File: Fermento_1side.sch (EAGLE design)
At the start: 25 parts, among them Q1 32.768kHz, Q2 P-MOSFET

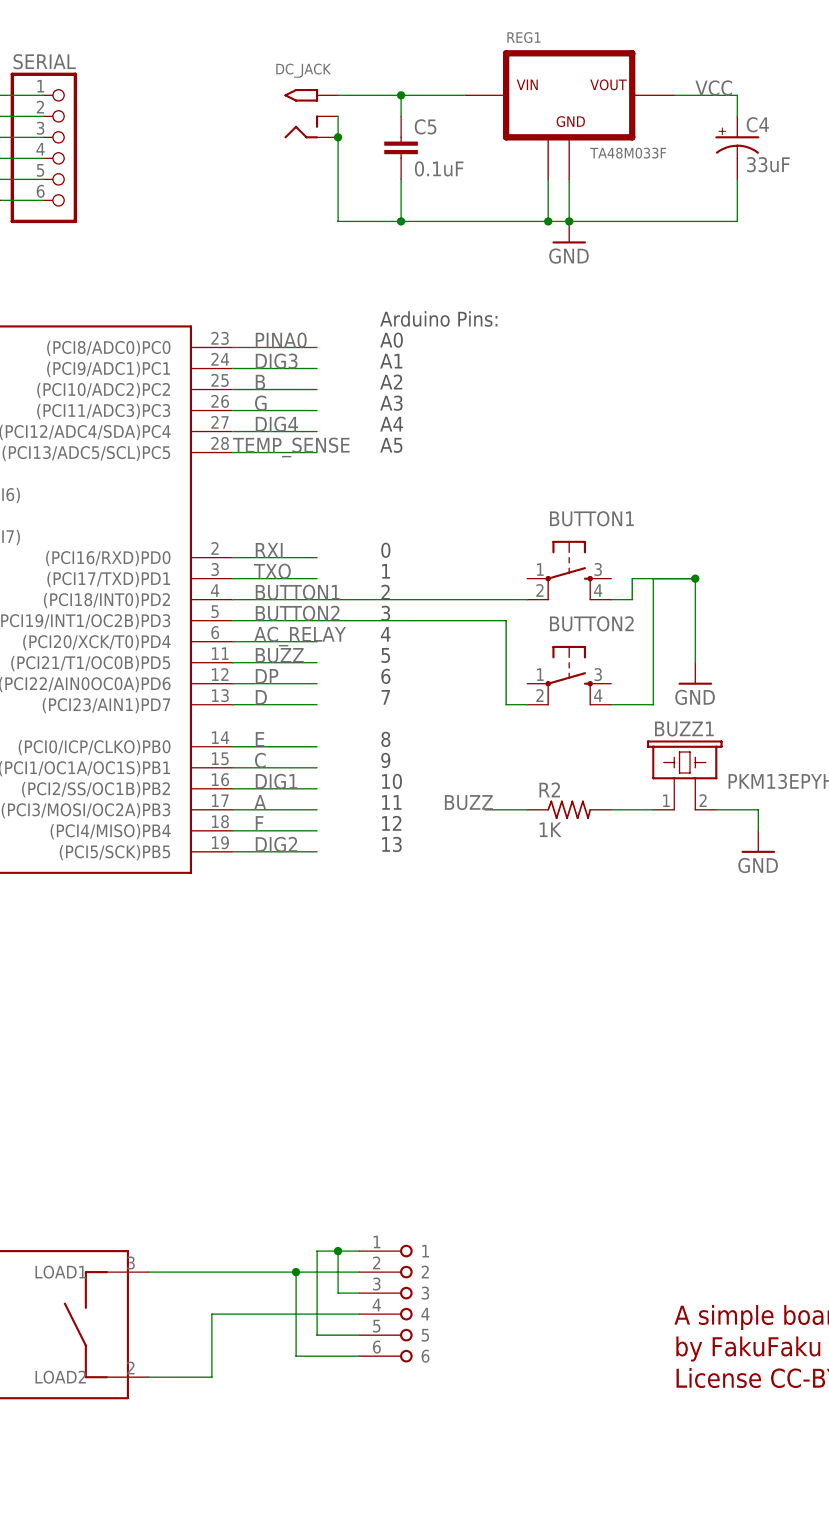
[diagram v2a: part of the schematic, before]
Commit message: One sided homebrew-friendly design redone.
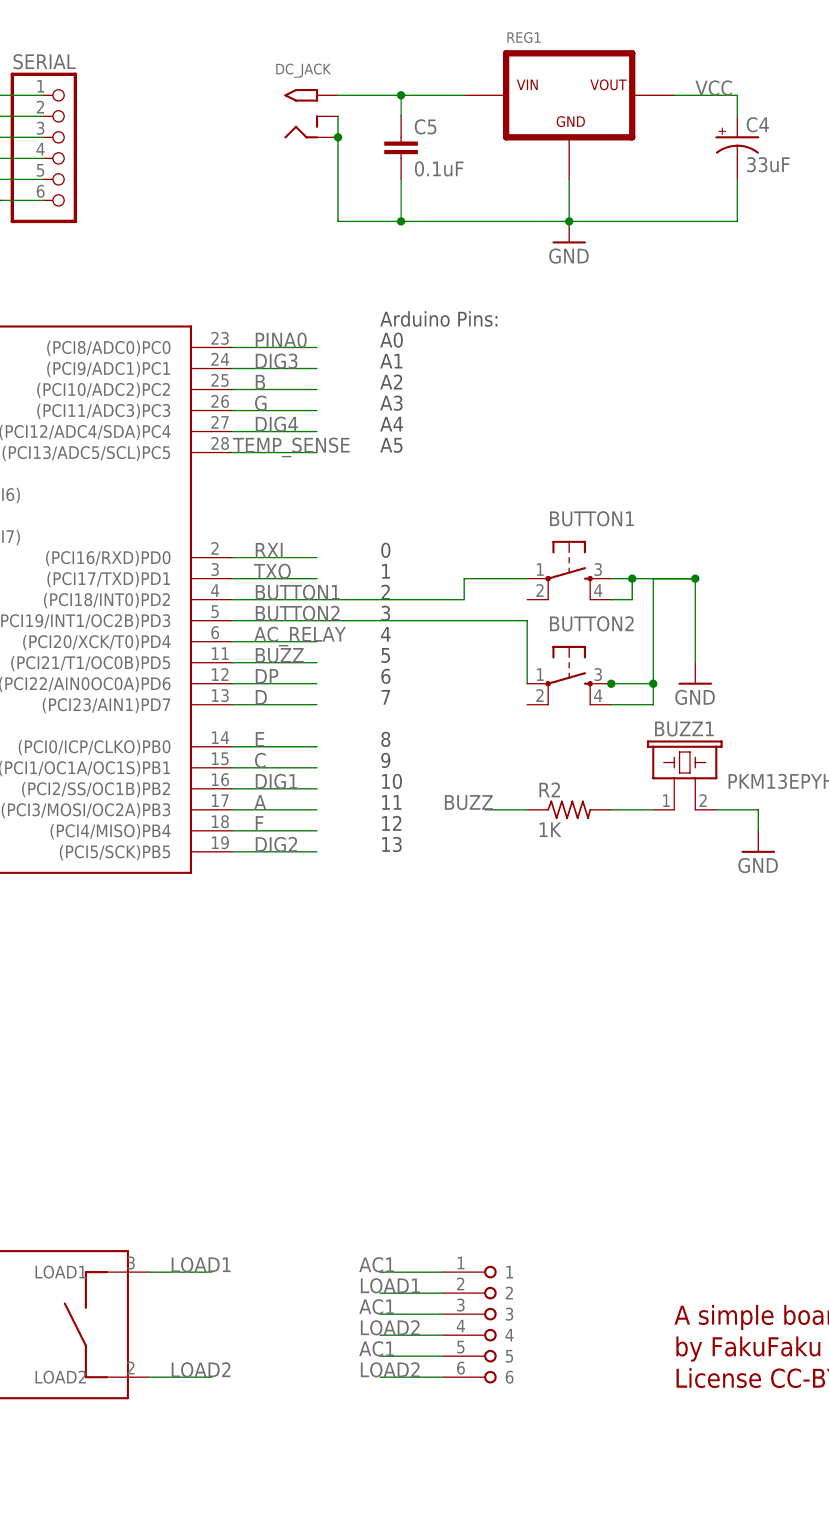
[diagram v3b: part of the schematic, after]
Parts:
- REG1: value TA48M033F -> REGULATOR-NOTHERMAL-TO220-STRAIGHT; device Robin:REGULATOR-TO-220 -> Robin:REGULATOR-NOTHERMAL-TO220-STRAIGHT
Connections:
- net N$5 renamed AC1
- removed net N$6: AC_RELAY.LOAD1, U$2.2, U$2.6
- removed net N$8: AC_RELAY.LOAD2, U$2.4
- new net LOAD1: AC_RELAY.LOAD1, U$2.2
- new net LOAD2: AC_RELAY.LOAD2, U$2.4, U$2.6
- net BUTTON1: now also BUTTON1.1; no longer BUTTON1.2
- net BUTTON2: now also BUTTON2.1; no longer BUTTON2.2
- net GND: now also BUTTON1.3, BUTTON2.3; no longer REG1.GND@1
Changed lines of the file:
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@@
 <part name="GND5" library="SparkFun" deviceset="GND" device=""/>
 <part name="GND6" library="SparkFun" deviceset="GND" device=""/>
-<part name="REG1" library="Robin" deviceset="REGULATOR" device="-TO-220" value="TA48M033F"/>
 <part name="C4" library="SparkFun" deviceset="CAP_POL" device="PTH2" value="33uF"/>
 <part name="C5" library="SparkFun" deviceset="CAP" device="PTH" value="0.1uF"/>
@@
 <part name="P+1" library="SparkFun" deviceset="VCC" device=""/>
 <part name="R3" library="adafruit" deviceset="R-US_" device="0207/10" value="10K"/>
+<part name="REG1" library="Robin" deviceset="REGULATOR-NOTHERMAL" device="-TO220-STRAIGHT" value=""/>
 </parts>
 <sheets>
@@
 <instance part="GND5" gate="1" x="231.14" y="-40.64"/>
 <instance part="GND6" gate="1" x="63.5" y="-27.94"/>
-<instance part="REG1" gate="G$1" x="154.94" y="-25.4"/>
 <instance part="C4" gate="G$1" x="175.26" y="-30.48"/>
 <instance part="C5" gate="G$1" x="134.62" y="-33.02"/>
@@
 <instance part="FRAME1" gate="G$2" x="165.1" y="-205.74"/>
 <instance part="AC_RELAY" gate="G$1" x="86.36" y="-175.26"/>
-<instance part="U$2" gate="G$1" x="134.62" y="-172.72"/>
+<instance part="U$2" gate="G$1" x="144.78" y="-175.26"/>
 <instance part="GND9" gate="1" x="66.04" y="-190.5"/>
 <instance part="H1" gate="G$1" x="55.88" y="-205.74"/>
@@
 <instance part="P+1" gate="1" x="55.88" y="-149.86"/>
 <instance part="R3" gate="G$1" x="40.64" y="-154.94" rot="R90"/>
+<instance part="REG1" gate="G$1" x="154.94" y="-25.4"/>
 </instances>
 <busses>
@@
 <pinref part="BUTTON2" gate="S" pin="4"/>
 <wire x1="160.02" y1="-99.06" x2="165.1" y2="-99.06" width="0.1524" layer="91"/>
-<wire x1="165.1" y1="-99.06" x2="165.1" y2="-83.82" width="0.1524" layer="91"/>
+<wire x1="165.1" y1="-99.06" x2="165.1" y2="-96.52" width="0.1524" layer="91"/>
+<wire x1="165.1" y1="-96.52" x2="165.1" y2="-83.82" width="0.1524" layer="91"/>
 <wire x1="165.1" y1="-83.82" x2="170.18" y2="-83.82" width="0.1524" layer="91"/>
 <pinref part="BUTTON1" gate="S" pin="4"/>
@@
 <wire x1="162.56" y1="-86.36" x2="162.56" y2="-83.82" width="0.1524" layer="91"/>
 <wire x1="162.56" y1="-83.82" x2="170.18" y2="-83.82" width="0.1524" layer="91"/>
+<junction x="162.56" y="-83.82"/>
+<junction x="165.1" y="-96.52"/>
+<pinref part="BUTTON2" gate="S" pin="3"/>
+<junction x="160.02" y="-96.52"/>
+<wire x1="160.02" y1="-96.52" x2="165.1" y2="-96.52" width="0.1524" layer="91"/>
+<pinref part="BUTTON1" gate="S" pin="3"/>
+<wire x1="162.56" y1="-83.82" x2="160.02" y2="-83.82" width="0.1524" layer="91"/>
 </segment>
 <segment>
@@
 <wire x1="175.26" y1="-40.64" x2="154.94" y2="-40.64" width="0.1524" layer="91"/>
 <wire x1="134.62" y1="-35.56" x2="134.62" y2="-40.64" width="0.1524" layer="91"/>
-<wire x1="134.62" y1="-40.64" x2="152.4" y2="-40.64" width="0.1524" layer="91"/>
-<wire x1="152.4" y1="-40.64" x2="154.94" y2="-40.64" width="0.1524" layer="91"/>
+<wire x1="134.62" y1="-40.64" x2="154.94" y2="-40.64" width="0.1524" layer="91"/>
 <wire x1="127" y1="-30.48" x2="127" y2="-40.64" width="0.1524" layer="91"/>
 <wire x1="127" y1="-40.64" x2="134.62" y2="-40.64" width="0.1524" layer="91"/>
 <wire x1="127" y1="-27.94" x2="127" y2="-30.48" width="0.1524" layer="91"/>
-<wire x1="152.4" y1="-35.56" x2="152.4" y2="-40.64" width="0.1524" layer="91"/>
 <junction x="154.94" y="-40.64"/>
 <junction x="134.62" y="-40.64"/>
 <junction x="127" y="-30.48"/>
-<junction x="152.4" y="-40.64"/>
 <pinref part="GND8" gate="1" pin="GND"/>
-<pinref part="REG1" gate="G$1" pin="GND"/>
 <pinref part="C4" gate="G$1" pin="-"/>
 <pinref part="C5" gate="G$1" pin="2"/>
 <pinref part="DC_JACK" gate="G$1" pin="RING"/>
 <pinref part="DC_JACK" gate="G$1" pin="RING_SW"/>
-<pinref part="REG1" gate="G$1" pin="GND@1"/>
+<pinref part="REG1" gate="G$1" pin="GND"/>
 </segment>
 <segment>
@@
 <wire x1="175.26" y1="-25.4" x2="175.26" y2="-27.94" width="0.1524" layer="91"/>
 <label x="170.18" y="-25.4" size="1.778" layer="95"/>
+<pinref part="C4" gate="G$1" pin="+"/>
 <pinref part="REG1" gate="G$1" pin="VOUT"/>
-<pinref part="C4" gate="G$1" pin="+"/>
 </segment>
 <segment>
@@
 <junction x="134.62" y="-25.4"/>
 <pinref part="DC_JACK" gate="G$1" pin="TIP"/>
+<pinref part="C5" gate="G$1" pin="1"/>
 <pinref part="REG1" gate="G$1" pin="VIN"/>
-<pinref part="C5" gate="G$1" pin="1"/>
 </segment>
 </net>
@@
 <pinref part="ATMEGA328" gate="G$1" pin="AREF"/>
 <pinref part="C1" gate="G$1" pin="1"/>
-</segment>
-</net>
-<net name="N$5" class="0">
-<segment>
-<pinref part="U$2" gate="G$1" pin="1"/>
-<wire x1="129.54" y1="-165.1" x2="127" y2="-165.1" width="0.1524" layer="91"/>
-<wire x1="127" y1="-165.1" x2="124.46" y2="-165.1" width="0.1524" layer="91"/>
-<wire x1="124.46" y1="-165.1" x2="124.46" y2="-175.26" width="0.1524" layer="91"/>
-<pinref part="U$2" gate="G$1" pin="5"/>
-<wire x1="124.46" y1="-175.26" x2="129.54" y2="-175.26" width="0.1524" layer="91"/>
-<junction x="127" y="-165.1"/>
-<pinref part="U$2" gate="G$1" pin="3"/>
-<wire x1="127" y1="-165.1" x2="127" y2="-170.18" width="0.1524" layer="91"/>
-<wire x1="127" y1="-170.18" x2="129.54" y2="-170.18" width="0.1524" layer="91"/>
-</segment>
-</net>
-<net name="N$6" class="0">
-<segment>
-<pinref part="U$2" gate="G$1" pin="2"/>
-<wire x1="129.54" y1="-167.64" x2="121.92" y2="-167.64" width="0.1524" layer="91"/>
-<wire x1="121.92" y1="-167.64" x2="121.92" y2="-177.8" width="0.1524" layer="91"/>
-<pinref part="U$2" gate="G$1" pin="6"/>
-<wire x1="121.92" y1="-177.8" x2="129.54" y2="-177.8" width="0.1524" layer="91"/>
-<junction x="121.92" y="-167.64"/>
-<wire x1="121.92" y1="-167.64" x2="104.14" y2="-167.64" width="0.1524" layer="91"/>
-<pinref part="AC_RELAY" gate="G$1" pin="LOAD1"/>
-</segment>
-</net>
-<net name="N$8" class="0">
-<segment>
-<pinref part="AC_RELAY" gate="G$1" pin="LOAD2"/>
-<wire x1="104.14" y1="-180.34" x2="111.76" y2="-180.34" width="0.1524" layer="91"/>
-<wire x1="111.76" y1="-180.34" x2="111.76" y2="-172.72" width="0.1524" layer="91"/>
-<pinref part="U$2" gate="G$1" pin="4"/>
-<wire x1="111.76" y1="-172.72" x2="129.54" y2="-172.72" width="0.1524" layer="91"/>
 </segment>
 </net>
@@
 </segment>
 </net>
-<net name="BUTTON1" class="0">
-<segment>
-<wire x1="114.3" y1="-86.36" x2="149.86" y2="-86.36" width="0.1524" layer="91"/>
-<label x="116.84" y="-86.36" size="1.778" layer="95"/>
-<pinref part="ATMEGA328" gate="G$1" pin="(PCI18/INT0)PD2"/>
-<pinref part="BUTTON1" gate="S" pin="2"/>
-</segment>
-</net>
 <net name="BUTTON2" class="0">
 <segment>
-<wire x1="114.3" y1="-88.9" x2="147.32" y2="-88.9" width="0.1524" layer="91"/>
+<wire x1="114.3" y1="-88.9" x2="149.86" y2="-88.9" width="0.1524" layer="91"/>
 <label x="116.84" y="-88.9" size="1.778" layer="95"/>
 <pinref part="ATMEGA328" gate="G$1" pin="(PCI19/INT1/OC2B)PD3"/>
-<pinref part="BUTTON2" gate="S" pin="2"/>
-<wire x1="147.32" y1="-88.9" x2="147.32" y2="-99.06" width="0.1524" layer="91"/>
-<wire x1="147.32" y1="-99.06" x2="149.86" y2="-99.06" width="0.1524" layer="91"/>
+<pinref part="BUTTON2" gate="S" pin="1"/>
+<wire x1="149.86" y1="-88.9" x2="149.86" y2="-96.52" width="0.1524" layer="91"/>
 </segment>
 </net>
@@
 </segment>
 </net>
+<net name="LOAD1" class="0">
+<segment>
+<pinref part="AC_RELAY" gate="G$1" pin="LOAD1"/>
+<wire x1="104.14" y1="-167.64" x2="111.76" y2="-167.64" width="0.1524" layer="91"/>
+<label x="106.68" y="-167.64" size="1.778" layer="95"/>
+</segment>
+<segment>
+<pinref part="U$2" gate="G$1" pin="2"/>
+<wire x1="139.7" y1="-170.18" x2="132.08" y2="-170.18" width="0.1524" layer="91"/>
+<label x="129.54" y="-170.18" size="1.778" layer="95"/>
+</segment>
+</net>
+<net name="LOAD2" class="0">
+<segment>
+<pinref part="AC_RELAY" gate="G$1" pin="LOAD2"/>
+<wire x1="104.14" y1="-180.34" x2="111.76" y2="-180.34" width="0.1524" layer="91"/>
+<label x="106.68" y="-180.34" size="1.778" layer="95"/>
+</segment>
+<segment>
+<pinref part="U$2" gate="G$1" pin="4"/>
+<wire x1="139.7" y1="-175.26" x2="132.08" y2="-175.26" width="0.1524" layer="91"/>
+<label x="129.54" y="-175.26" size="1.778" layer="95"/>
+</segment>
+<segment>
+<pinref part="U$2" gate="G$1" pin="6"/>
+<wire x1="139.7" y1="-180.34" x2="132.08" y2="-180.34" width="0.1524" layer="91"/>
+<label x="129.54" y="-180.34" size="1.778" layer="95"/>
+</segment>
+</net>
+<net name="AC1" class="0">
+<segment>
+<pinref part="U$2" gate="G$1" pin="3"/>
+<wire x1="139.7" y1="-172.72" x2="132.08" y2="-172.72" width="0.1524" layer="91"/>
+<label x="129.54" y="-172.72" size="1.778" layer="95"/>
+</segment>
+<segment>
+<pinref part="U$2" gate="G$1" pin="5"/>
+<wire x1="139.7" y1="-177.8" x2="132.08" y2="-177.8" width="0.1524" layer="91"/>
+<label x="129.54" y="-177.8" size="1.778" layer="95"/>
+</segment>
+<segment>
+<pinref part="U$2" gate="G$1" pin="1"/>
+<wire x1="139.7" y1="-167.64" x2="132.08" y2="-167.64" width="0.1524" layer="91"/>
+<label x="129.54" y="-167.64" size="1.778" layer="95"/>
+</segment>
+</net>
+<net name="BUTTON1" class="0">
+<segment>
+<pinref part="ATMEGA328" gate="G$1" pin="(PCI18/INT0)PD2"/>
+<wire x1="114.3" y1="-86.36" x2="142.24" y2="-86.36" width="0.1524" layer="91"/>
+<wire x1="142.24" y1="-86.36" x2="142.24" y2="-83.82" width="0.1524" layer="91"/>
+<pinref part="BUTTON1" gate="S" pin="1"/>
+<wire x1="142.24" y1="-83.82" x2="149.86" y2="-83.82" width="0.1524" layer="91"/>
+<label x="116.84" y="-86.36" size="1.778" layer="95"/>
+</segment>
+</net>
